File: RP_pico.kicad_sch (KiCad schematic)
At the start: 46 parts, among them J17 Conn_01x03_MountingPin, SW1 SW_Push, SW2 SW_Push, U12 W25Q128JVE, U3 RP2350A, Y1 Crystal_GND24

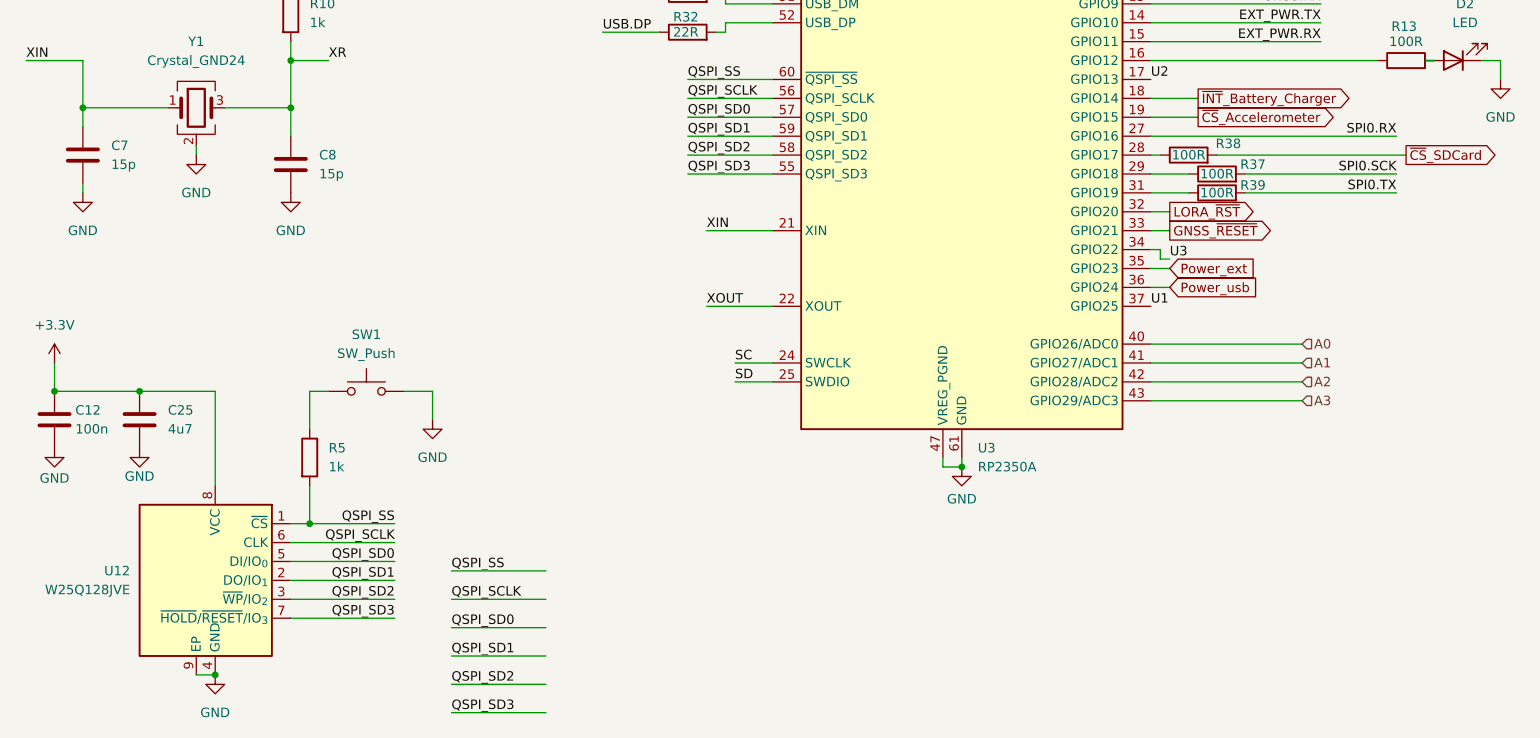
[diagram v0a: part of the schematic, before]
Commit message: PCB updates
Update miscellaneous.kicad_sch to add new fiducial symbol and replace existing fiducial references

- Added a new fiducial symbol "BC_Miscellaneous:Fiducial" with ground
- Updated references in the schematic to point to the new fiducial symbol.

- Changed the DNP (Do Not Place) property for components U13 and U6 from 'no' to 'yes' to prevent placement on the PCB.
- Updated the footprint property for U13 to "BC_Memory:W25Q" to reflect the correct component footprint.
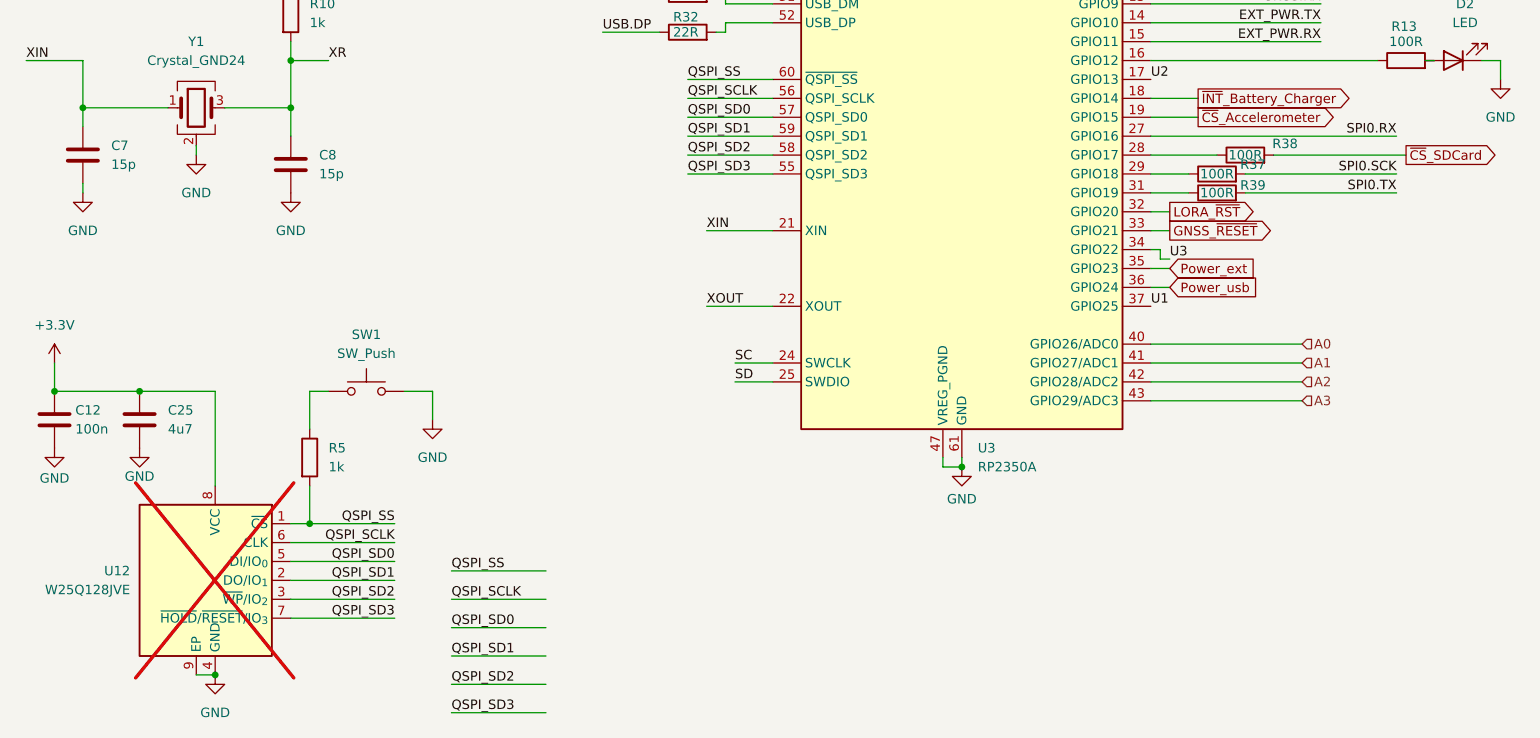
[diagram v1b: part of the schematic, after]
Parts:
- U12: footprint Package_SON:WSON-8-1EP_8x6mm_P1.27mm_EP3.4x4.3mm -> BC_Memory:W25Q; now not fitted
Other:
- moved on the sheet: R38
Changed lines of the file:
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@@
 	(wire
 		(pts
-			(xy 102.87 109.22) (xy 114.3 109.22)
+			(xy 165.1 119.38) (xy 173.99 119.38)
 		)
 		(stroke
@@
 	(wire
 		(pts
-			(xy 127 43.18) (xy 116.84 43.18)
+			(xy 102.87 109.22) (xy 114.3 109.22)
 		)
 		(stroke
@@
 	(wire
 		(pts
-			(xy 165.1 101.6) (xy 187.96 101.6)
+			(xy 127 43.18) (xy 116.84 43.18)
 		)
 		(stroke
@@
 	(wire
 		(pts
-			(xy 165.1 119.38) (xy 166.37 119.38)
+			(xy 165.1 101.6) (xy 187.96 101.6)
 		)
 		(stroke
@@
 	(wire
 		(pts
+			(xy 181.61 119.38) (xy 199.39 119.38)
+		)
+		(stroke
+			(width 0)
+			(type default)
+		)
+	)
+	(wire
+		(pts
 			(xy 129.54 63.5) (xy 127 63.5)
 		)
@@
 	(wire
 		(pts
-			(xy 173.99 119.38) (xy 199.39 119.38)
-		)
-		(stroke
-			(width 0)
-			(type default)
-		)
-	)
-	(wire
-		(pts
 			(xy 102.87 114.3) (xy 114.3 114.3)
 		)
@@
 		(length 2.54)
 		(shape round)
-		(at 180.34 119.38 0)
+		(at 187.96 119.38 0)
 		(fields_autoplaced yes)
 		(effects
@@
 		)
 		(property "Netclass" "Signal"
-			(at 180.9496 116.84 0)
+			(at 188.5696 116.84 0)
 			(show_name no)
 			(do_not_autoplace no)
@@
 		)
 		(property "Component Class" ""
-			(at 199.39 104.14 0)
+			(at 207.01 104.14 0)
 			(show_name no)
 			(do_not_autoplace no)
@@
 		(on_board yes)
 		(in_pos_files yes)
-		(dnp no)
+		(dnp yes)
 		(property "Reference" "U12"
 			(at 27.94 175.2599 0)
@@
 			)
 		)
-		(property "Footprint" "Package_SON:WSON-8-1EP_8x6mm_P1.27mm_EP3.4x4.3mm"
+		(property "Footprint" "BC_Memory:W25Q"
 			(at 39.37 153.67 0)
 			(hide yes)
@@
 		(instances
 			(project "PowerLineSensorPCB"
+				(path "/6b3d7a89-016e-44cc-aa76-b24fbbba08cf/14b821c4-7c41-42c4-a587-dc590b7e8e40"
+					(reference "U12")
+					(unit 1)
+				)
 				(path "/6b3d7a89-016e-44cc-aa76-b24fbbba08cf/eec70212-a38a-46df-9214-2ed1263aeba7"
 					(reference "U12")
@@
 	(symbol
 		(lib_id "Device:R")
-		(at 170.18 119.38 90)
+		(at 177.8 119.38 90)
 		(unit 1)
 		(body_style 1)
@@
 		(dnp no)
 		(property "Reference" "R38"
-			(at 175.514 117.856 90)
+			(at 183.134 117.856 90)
 			(show_name no)
 			(do_not_autoplace no)
@@
 		)
 		(property "Value" "100R"
-			(at 170.18 119.38 90)
+			(at 177.8 119.38 90)
 			(show_name no)
 			(do_not_autoplace no)
@@
 		)
 		(property "Footprint" "Resistor_SMD:R_0402_1005Metric"
-			(at 170.18 121.158 90)
+			(at 177.8 121.158 90)
 			(hide yes)
 			(show_name no)
@@
 		)
 		(property "Datasheet" ""
-			(at 170.18 119.38 0)
+			(at 177.8 119.38 0)
 			(hide yes)
 			(show_name no)
@@
 		)
 		(property "Description" "Resistor"
-			(at 170.18 119.38 0)
+			(at 177.8 119.38 0)
 			(hide yes)
 			(show_name no)
@@
 		)
 		(property "PartNumber" "0402WGF1000TCE"
-			(at 170.18 119.38 90)
+			(at 177.8 119.38 90)
 			(hide yes)
 			(show_name no)
@@
 		)
 		(property "KLC_S4.2_DVDD" ""
-			(at 170.18 119.38 90)
+			(at 177.8 119.38 90)
 			(hide yes)
 			(show_name no)
@@
 		)
 		(property "KLC_S4.2_VREG_LX" ""
-			(at 170.18 119.38 90)
+			(at 177.8 119.38 90)
 			(hide yes)
 			(show_name no)
@@
 		)
 		(property "KLC_S3.3" ""
-			(at 170.18 119.38 90)
+			(at 177.8 119.38 90)
 			(hide yes)
 			(show_name no)
@@
 		)
 		(property "KLC_S4.1" ""
-			(at 170.18 119.38 90)
+			(at 177.8 119.38 90)
 			(hide yes)
 			(show_name no)

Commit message: send to production. v0.1, making jobset for export
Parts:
- U12: PartNumber W25Q128JVEIM -> W25Q128JVEIM
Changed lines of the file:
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@@
 	(generator_version "10.0")
 	(paper "A4")
+	(title_block
+		(rev "${Revision}")
+	)
 	(rectangle
 		(start 139.7 22.86)
@@
 	(wire
 		(pts
-			(xy 165.1 127) (xy 167.64 127)
+			(xy 165.1 127) (xy 180.34 127)
 		)
 		(stroke
@@
 	(wire
 		(pts
-			(xy 248.92 81.28) (xy 265.43 81.28)
-		)
-		(stroke
-			(width 0)
-			(type default)
-		)
-	)
-	(wire
-		(pts
 			(xy 152.4 43.18) (xy 157.48 43.18)
 		)
@@
 		)
 	)
-	(label "EN_hall"
-		(at 248.92 81.28 0)
-		(effects
-			(font
-				(size 1.27 1.27)
-			)
-			(justify left bottom)
-		)
-	)
 	(label "QSPI_SS"
 		(at 63.5 168.91 180)
@@
 	(global_label "LORA_~{RST}"
 		(shape output)
-		(at 167.64 127 0)
+		(at 180.34 127 0)
 		(fields_autoplaced yes)
 		(effects
@@
 		)
 		(property "Intersheetrefs" "${INTERSHEET_REFS}"
-			(at 179.7571 127 0)
+			(at 192.4571 127 0)
 			(hide yes)
 			(show_name no)
@@
 		)
 	)
-	(hierarchical_label "EN_hall"
-		(shape output)
-		(at 265.43 81.28 0)
-		(effects
-			(font
-				(size 1.27 1.27)
-			)
-			(justify left)
-		)
-	)
 	(hierarchical_label "A3"
 		(shape input)
@@
 			)
 		)
-		(property "PartNumber" "W25Q128JVEIM "
+		(property "PartNumber" "W25Q128JVEIM"
 			(at 39.37 176.53 0)
 			(hide yes)
@@
 		(instances
 			(project "PowerLineSensorPCB"
-				(path "/6b3d7a89-016e-44cc-aa76-b24fbbba08cf/14b821c4-7c41-42c4-a587-dc590b7e8e40"
-					(reference "U12")
-					(unit 1)
-				)
 				(path "/6b3d7a89-016e-44cc-aa76-b24fbbba08cf/eec70212-a38a-46df-9214-2ed1263aeba7"
 					(reference "U12")
